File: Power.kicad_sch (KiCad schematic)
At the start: 8 parts, among them U3 AZ1117EH-3.3, U6 DNP-AZ1117CH2-3.3

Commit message: Toward final "A"
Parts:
- renumbered U6 to U4
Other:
- moved on the sheet: C3, C4

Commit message: final version?
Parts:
- removed U4: DNP-AZ1117CH2-3.3, stdpads:SOT-223, symbol GW_Power:AZ1117CH2
- U3: value AZ1117EH-3.3 -> AZ1117CH-3.3

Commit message: RC
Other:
- company: (none) -> Garrett's Workshop
- title: (none) -> WarpSE (GW4410A)
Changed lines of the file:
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@@
 (kicad_sch (version 20230121) (generator eeschema)
   (paper "A4")
+  (title_block
+    (title "WarpSE (GW4410A)")
+    (date "2024-03-27")
+    (rev "1.0")
+    (company "Garrett's Workshop")
+  )
   (junction (at 153.67 60.96) (diameter 0) (color 0 0 0 0)
   )

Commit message: RC
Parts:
- U3: value AZ1117CH-3.3 -> AZ1117CH-3.3TRG1; LCSC Part C108494 -> C92102
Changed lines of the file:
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@@
   (title_block
     (title "WarpSE (GW4410A)")
-    (date "2024-03-27")
+    (date "2024-04-23")
     (rev "1.0")
     (company "Garrett's Workshop")
@@
       (effects (font (size 1.27 1.27)))
     )
-    (property "Value" "AZ1117CH-3.3" (at 133.35 50.8 0)
+    (property "Value" "AZ1117CH-3.3TRG1" (at 133.35 50.8 0)
       (effects (font (size 1.27 1.27)) (justify bottom))
     )
@@
       (effects (font (size 1.27 1.27)) hide)
     )
-    (property "Datasheet" "http://www.diodes.com/datasheets/AP1117.pdf" (at 135.89 59.69 0)
-      (effects (font (size 1.27 1.27)) hide)
-    )
-    (property "LCSC Part" "C108494" (at 133.35 53.34 0)
+    (property "Datasheet" "" (at 135.89 59.69 0)
+      (effects (font (size 1.27 1.27)) hide)
+    )
+    (property "LCSC Part" "C92102" (at 133.35 53.34 0)
       (effects (font (size 1.27 1.27)) hide)
     )
@@
       (effects (font (size 1.27 1.27)) hide)
     )
-    (property "Datasheet" "~" (at 118.11 57.15 0)
+    (property "Datasheet" "" (at 118.11 57.15 0)
       (effects (font (size 1.27 1.27)) hide)
     )
@@
       (effects (font (size 1.27 1.27)) hide)
     )
-    (property "Datasheet" "~" (at 143.51 57.15 0)
+    (property "Datasheet" "" (at 143.51 57.15 0)
       (effects (font (size 1.27 1.27)) hide)
     )
@@
       (effects (font (size 1.27 1.27)) hide)
     )
-    (property "Datasheet" "~" (at 153.67 57.15 0)
+    (property "Datasheet" "" (at 153.67 57.15 0)
       (effects (font (size 1.27 1.27)) hide)
     )
@@
       (effects (font (size 1.27 1.27)) hide)
     )
-    (property "Datasheet" "~" (at 163.83 57.15 0)
+    (property "Datasheet" "" (at 163.83 57.15 0)
       (effects (font (size 1.27 1.27)) hide)
     )
@@
       (effects (font (size 1.27 1.27)) hide)
     )
-    (property "Datasheet" "~" (at 107.95 57.15 0)
+    (property "Datasheet" "" (at 107.95 57.15 0)
       (effects (font (size 1.27 1.27)) hide)
     )
@@
       (effects (font (size 1.27 1.27)) hide)
     )
-    (property "Datasheet" "~" (at 173.99 57.15 0)
-      (effects (font (size 1.27 1.27)) hide)
-    )
+    (property "Datasheet" "" (at 173.99 57.15 0)
+      (effects (font (size 1.27 1.27)) hide)
+    )

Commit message: USB power
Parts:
- added U4: MAX40200AUK, stdpads:SOT-353, symbol GW_Power:MAX40200AUK
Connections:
- net +5V: now also U4.5 (Vout)
- net GND: now also U4.2 (GND)
- new net +5Vin: U4.1 (Vin), U4.3 (En)
- no-connect marks 0 -> 1

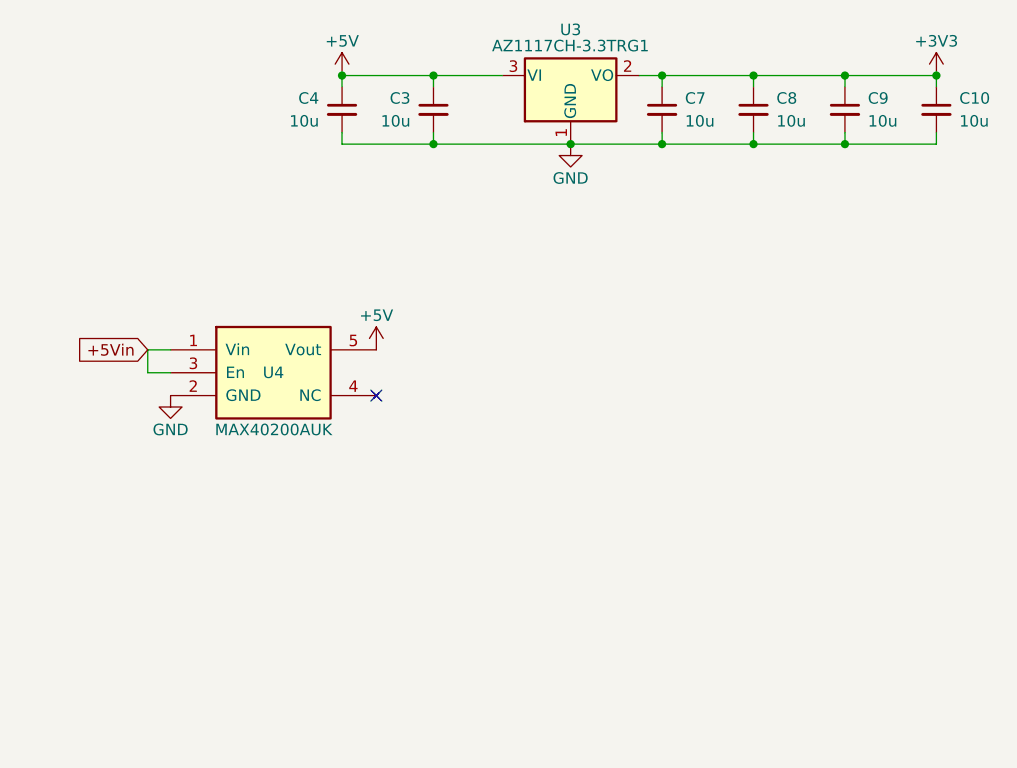
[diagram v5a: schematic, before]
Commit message: Add LM66100 instead of MAX40200AUK
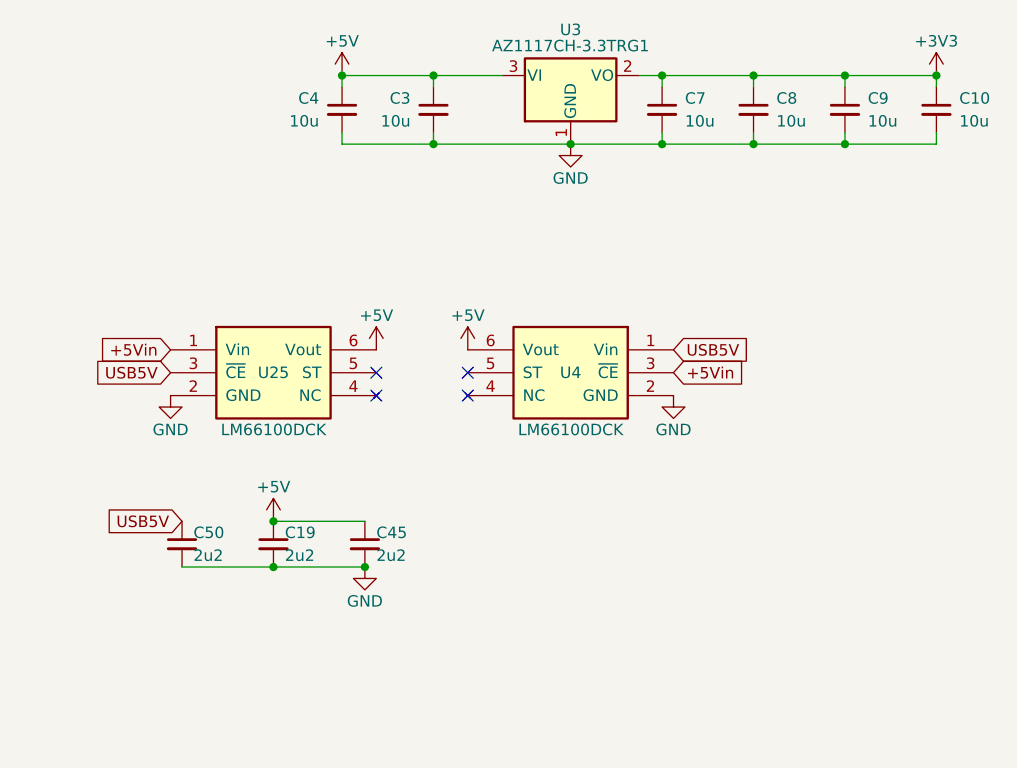
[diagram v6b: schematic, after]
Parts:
- removed U4: MAX40200AUK, stdpads:SOT-353, symbol GW_Power:MAX40200AUK
- added C19, C45, C50: 2u2, stdpads:C_0603, symbol Device:C_Small
- added U25, U4: LM66100DCK, stdpads:SOT-363, symbol GW_Power:LM66100DCK
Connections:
- net +5V: now also C19.1, C45.1, U25.6 (Vout), U4.6 (Vout)
- net +5Vin: now also U25.1 (Vin), U4.3 (~{CE})
- net GND: now also C19.2, C45.2, C50.2, U25.2 (GND), U4.2 (GND)
- new net USB5V: C50.1, U25.3 (~{CE}), U4.1 (Vin)
- no-connect marks 1 -> 4

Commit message: Board prerelease revision 3 with USB power, A[23:20] remapping
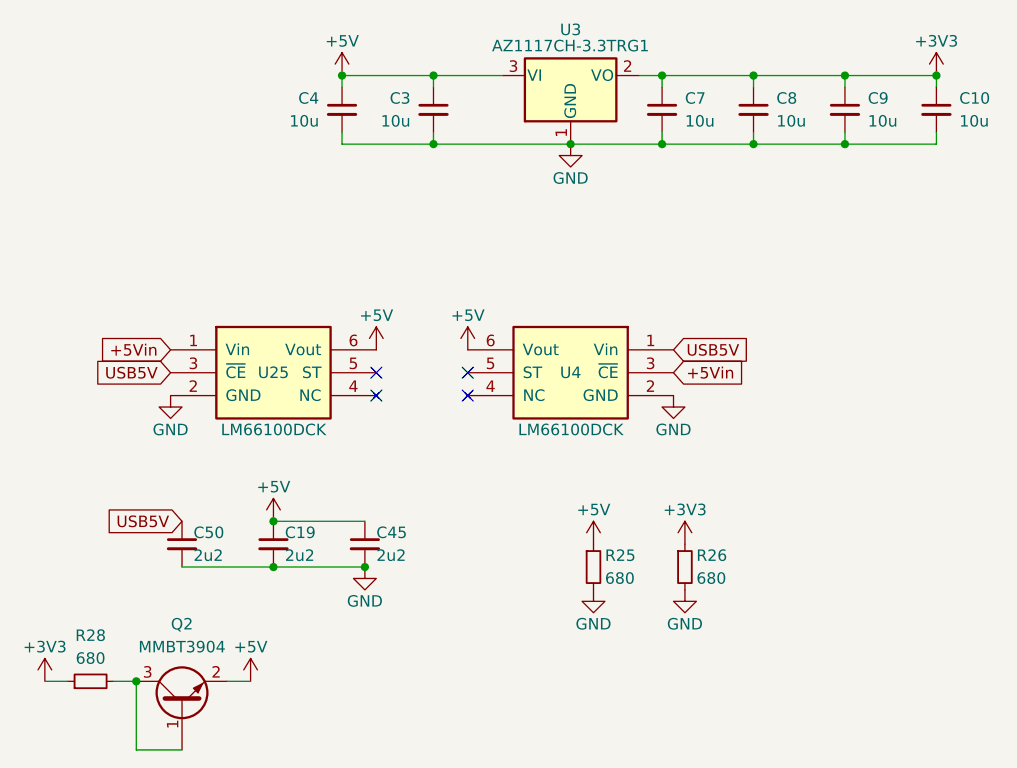
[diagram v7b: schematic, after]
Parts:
- added Q2: MMBT3904, stdpads:SOT-23, symbol Transistor_BJT:MMBT3904
- added R25, R26, R28: 680, stdpads:R_0805, symbol Device:R_Small
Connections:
- net +3V3: now also R26.1, R28.1
- net +5V: now also Q2.2 (E), R25.1
- net GND: now also R25.2, R26.2
- new net: Q2.1 (B), Q2.3 (C), R28.2

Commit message: Before switching to SiT2001 oscillator
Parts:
- added R27: 680, stdpads:R_0805, symbol Device:R_Small
- Q2: value MMBT3904 -> DNP
- R28: value 680 -> DNP
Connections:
- net +5Vin: now also R27.1
- net GND: now also R27.2
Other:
- moved on the sheet: R25, R26
